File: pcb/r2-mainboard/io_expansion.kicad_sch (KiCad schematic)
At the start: 16 parts, among them J1400 HC-FPC-05-09-6RLTAG, J1401 HC-FPC-05-09-6RLTAG, J1402 USB-C 16P, U1400 TPS22914BYFPR, U1401 TPS22914BYFPR, U1402 TPS2553DBVR, U1403 USBLC6-2SC6

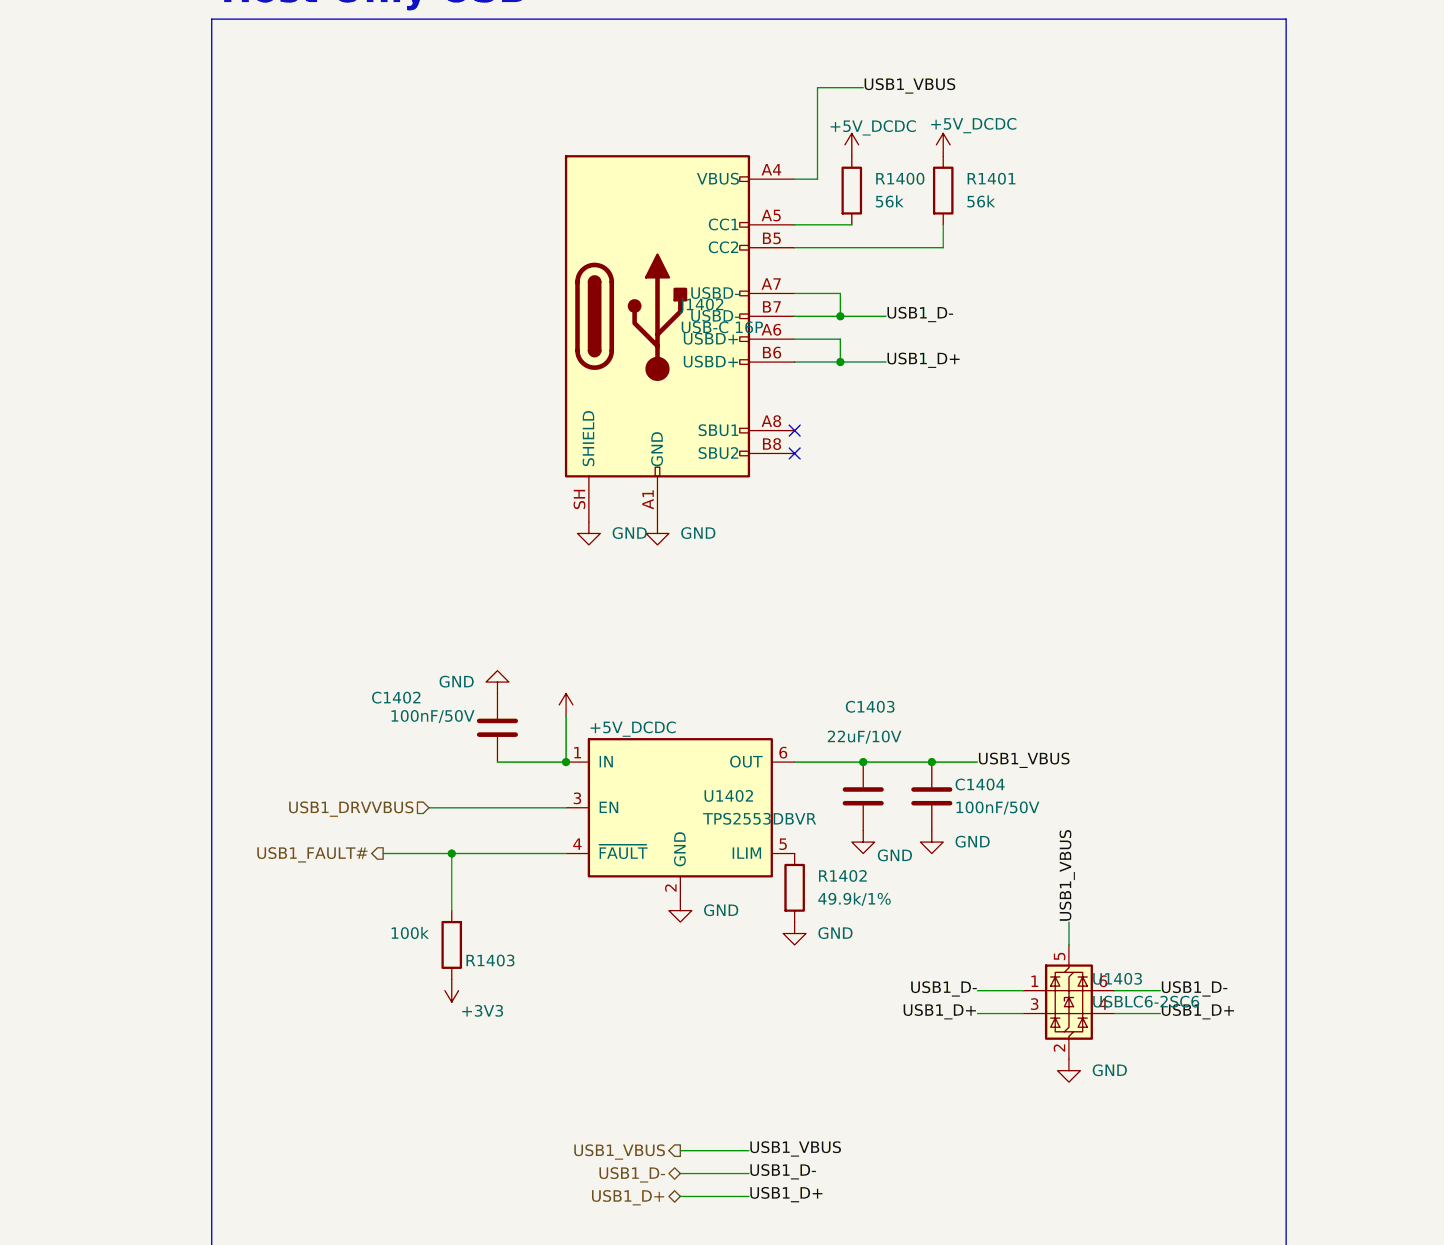
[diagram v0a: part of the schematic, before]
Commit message: changing to osb62x-pm
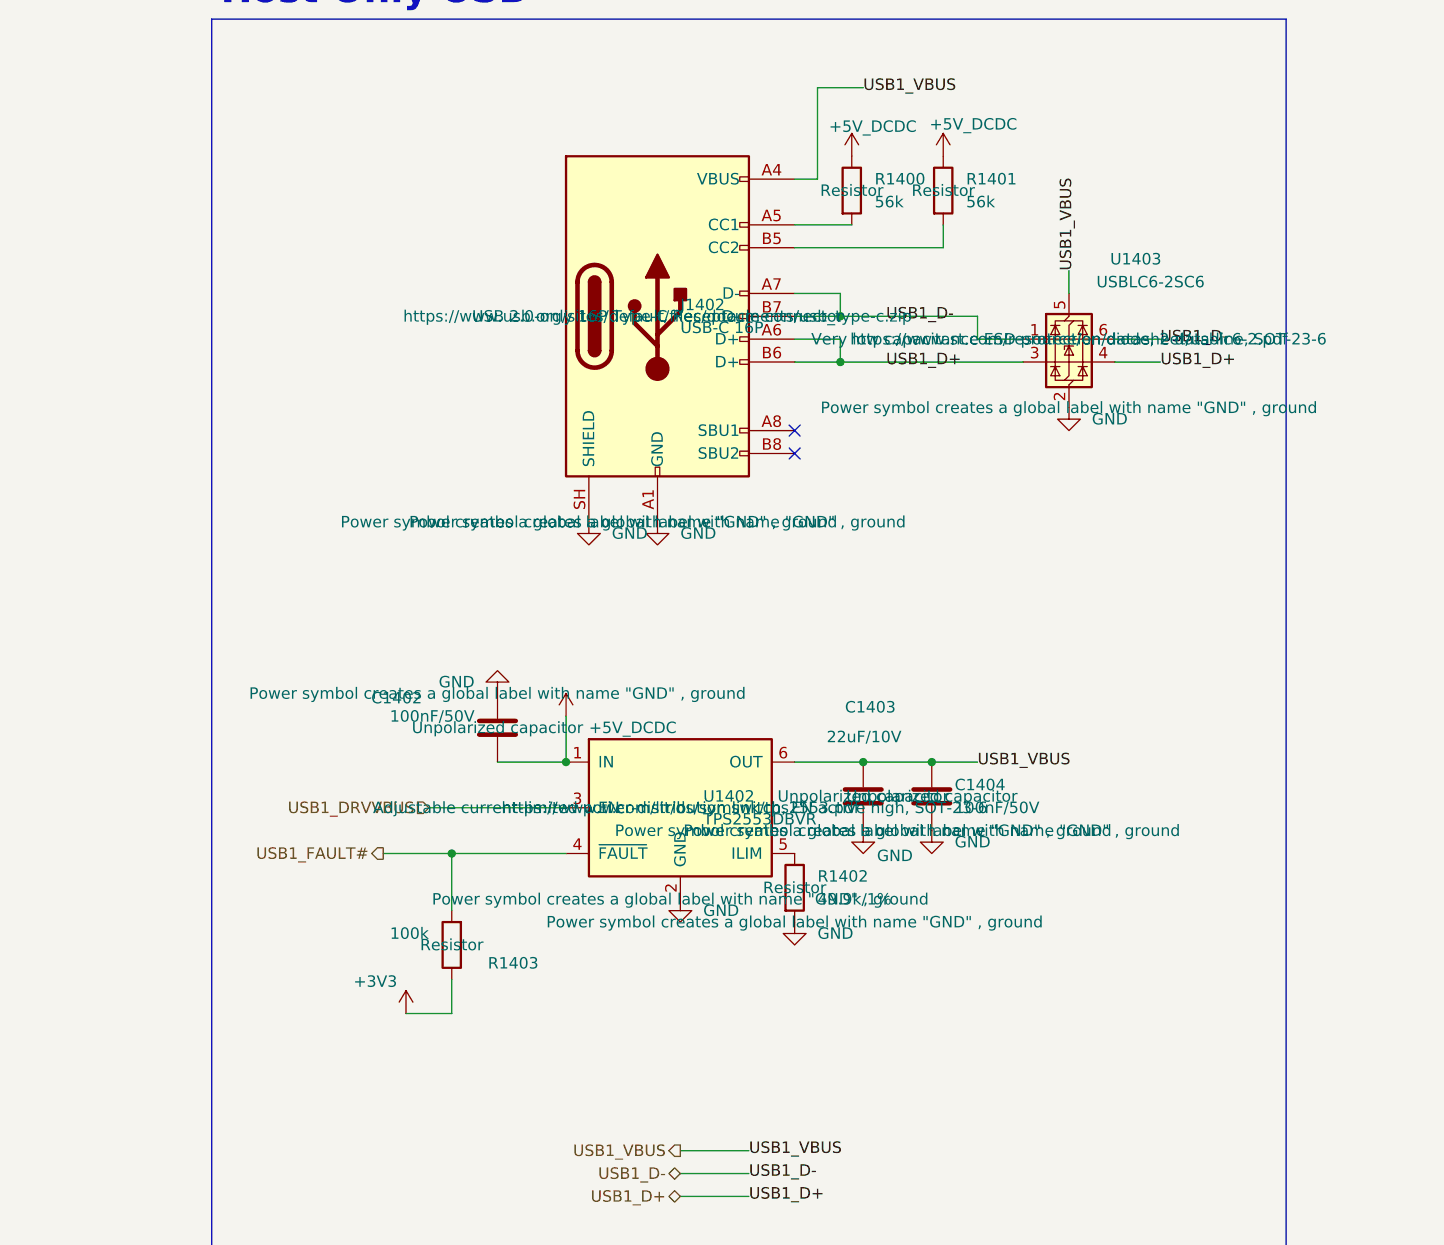
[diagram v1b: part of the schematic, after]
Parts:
- U1400, U1401: footprint Package_BGA:WLP-4_0.83x0.83mm_P0.4mm -> Package_CSP:WLCSP-4_0.89x0.89mm_Layout2x2_P0.5mm
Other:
- moved on the sheet: U1403

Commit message: Schematics update for new chip.
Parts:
- added U600: OSD6254-1G-IPM, Reflow:BGA500C50P28X18_1400X900X130, symbol Reflow:OSD6254-1G-IPM
- C1400, C1401: value 1uF/16V -> 1uF/25V
- C1403: value 22uF/10V -> 22uF/25V
- R1400, R1401: value 56k -> 56k/1%
- R1403: value 100k -> 100k/1%
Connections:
- net USB1_D+: now also U600.V10 (USB1_DP)
- net USB1_D-: now also U600.U10 (USB1_DM)
- net USB1_VBUS: now also U600.U11 (USB1_VBUS)
